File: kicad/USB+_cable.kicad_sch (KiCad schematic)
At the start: 2 parts, among them J1601 USB_C_Receptacle, J1602 USB_C_Receptacle

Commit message: Broke down sensor block into a tree of sheets
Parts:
- added D1601: GREEN, YELLOW, KwanSystems:LEDKingbrightAPHB, symbol Device:LED_Dual_AKAK
- added R1601: 330, Resistor_SMD:R_0402_1005Metric, symbol KwanSystems:RESISTOR
- added R1602: 1k, Resistor_SMD:R_0402_1005Metric, symbol KwanSystems:RESISTOR
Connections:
- net P_3V3: now also D1601.1 (A1), R1602.2
- net P_GND: now also R1601.2
- net P_ID: now also D1601.3 (A2)
- new net DG-: D1601.2 (K1), R1601.1
- new net DY-: D1601.4 (K2), R1602.1
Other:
- note added: "Will light GREEN if HI board (green=higher energy photon) YELLOW if LO board (yellow=lower energy photon) Neither color is red, so no danger/stop indication"
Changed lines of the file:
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@@
 (kicad_sch (version 20211123) (generator eeschema)
   (paper "A4")
+  (junction (at 124.46 119.38) (diameter 0) (color 0 0 0 0)
+  )
   (junction (at 213.36 129.54) (diameter 0) (color 0 0 0 0)
   )
+  (junction (at 134.62 119.38) (diameter 0) (color 0 0 0 0)
+  )
+  (junction (at 119.38 129.54) (diameter 0) (color 0 0 0 0)
+  )
   (junction (at 228.6 78.74) (diameter 0) (color 0 0 0 0)
+  )
+  (junction (at 129.54 114.3) (diameter 0) (color 0 0 0 0)
   )
   (junction (at 228.6 81.28) (diameter 0) (color 0 0 0 0)
@@
     (stroke (width 0) (type default) (color 0 0 0 0))
   )
+  (wire (pts (xy 134.62 119.38) (xy 124.46 119.38))
+    (stroke (width 0) (type default) (color 0 0 0 0))
+  )
   (polyline (pts (xy 165.1 121.92) (xy 177.8 121.92))
     (stroke (width 0) (type solid) (color 0 0 0 0))
@@
     (stroke (width 0) (type solid) (color 0 0 0 0))
   )
+  (wire (pts (xy 119.38 129.54) (xy 119.38 139.7))
+    (stroke (width 0) (type default) (color 0 0 0 0))
+  )
   (polyline (pts (xy 177.8 68.58) (xy 177.8 69.85))
     (stroke (width 0) (type solid) (color 0 0 0 0))
@@
     (stroke (width 0) (type default) (color 0 0 0 0))
   )
+  (wire (pts (xy 129.54 154.94) (xy 134.62 154.94))
+    (stroke (width 0) (type default) (color 0 0 0 0))
+  )
   (polyline (pts (xy 165.1 106.68) (xy 177.8 106.68))
     (stroke (width 0) (type solid) (color 0 0 0 0))
@@
     (stroke (width 0) (type default) (color 0 0 0 0))
   )
-  (wire (pts (xy 139.7 119.38) (xy 114.3 119.38))
+  (wire (pts (xy 124.46 119.38) (xy 114.3 119.38))
+    (stroke (width 0) (type default) (color 0 0 0 0))
+  )
+  (wire (pts (xy 139.7 119.38) (xy 134.62 119.38))
     (stroke (width 0) (type default) (color 0 0 0 0))
   )
@@
     (stroke (width 0) (type default) (color 0 0 0 0))
   )
+  (wire (pts (xy 134.62 119.38) (xy 134.62 139.7))
+    (stroke (width 0) (type default) (color 0 0 0 0))
+  )
+  (wire (pts (xy 119.38 154.94) (xy 124.46 154.94))
+    (stroke (width 0) (type default) (color 0 0 0 0))
+  )
+  (wire (pts (xy 124.46 119.38) (xy 124.46 139.7))
+    (stroke (width 0) (type default) (color 0 0 0 0))
+  )
   (wire (pts (xy 228.6 114.3) (xy 254 114.3))
     (stroke (width 0) (type default) (color 0 0 0 0))
@@
     (stroke (width 0) (type solid) (color 0 0 0 0))
   )
-  (wire (pts (xy 114.3 114.3) (xy 139.7 114.3))
+  (wire (pts (xy 134.62 154.94) (xy 134.62 144.78))
+    (stroke (width 0) (type default) (color 0 0 0 0))
+  )
+  (wire (pts (xy 114.3 114.3) (xy 129.54 114.3))
     (stroke (width 0) (type default) (color 0 0 0 0))
   )
@@
     (stroke (width 0) (type solid) (color 0 0 0 0))
   )
+  (wire (pts (xy 119.38 144.78) (xy 119.38 154.94))
+    (stroke (width 0) (type default) (color 0 0 0 0))
+  )
+  (wire (pts (xy 129.54 114.3) (xy 129.54 139.7))
+    (stroke (width 0) (type default) (color 0 0 0 0))
+  )
   (polyline (pts (xy 177.8 114.3) (xy 190.5 106.68))
     (stroke (width 0) (type solid) (color 0 0 0 0))
@@
     (stroke (width 0) (type default) (color 0 0 0 0))
   )
-  (wire (pts (xy 114.3 129.54) (xy 154.94 129.54))
+  (wire (pts (xy 114.3 129.54) (xy 119.38 129.54))
     (stroke (width 0) (type default) (color 0 0 0 0))
   )
@@
     (stroke (width 0) (type solid) (color 0 0 0 0))
   )
+  (wire (pts (xy 129.54 114.3) (xy 139.7 114.3))
+    (stroke (width 0) (type default) (color 0 0 0 0))
+  )
   (wire (pts (xy 228.6 121.92) (xy 254 121.92))
+    (stroke (width 0) (type default) (color 0 0 0 0))
+  )
+  (wire (pts (xy 119.38 129.54) (xy 154.94 129.54))
     (stroke (width 0) (type default) (color 0 0 0 0))
   )
@@
   )
   (text "BRAID" (at 181.61 125.73 0)
+    (effects (font (size 1.27 1.27)) (justify left bottom))
+  )
+  (text "Will light GREEN if HI board (green=higher energy photon)\nYELLOW if LO board (yellow=lower energy photon)\nNeither color is red, so no danger/stop indication"
+    (at 140.97 158.75 0)
     (effects (font (size 1.27 1.27)) (justify left bottom))
   )
@@
   )
   (text "WHITE(GREEN MYLAR)" (at 165.1 111.76 0)
+    (effects (font (size 1.27 1.27)) (justify left bottom))
+  )
+  (label "DY-" (at 134.62 154.94 90)
+    (effects (font (size 1.27 1.27)) (justify left bottom))
+  )
+  (label "DG-" (at 119.38 154.94 90)
     (effects (font (size 1.27 1.27)) (justify left bottom))
   )
@@
     (pin "S1")
   )
+  (symbol (lib_id "Device:LED_Dual_AKAK") (at 127 147.32 90) (mirror x)
+    (in_bom yes) (on_board yes)
+    (property "Reference" "D1601" (id 0) (at 124.46 156.21 90)
+      (effects (font (size 1.27 1.27)) (justify right))
+    )
+    (property "Value" "GREEN, YELLOW" (id 1) (at 120.65 158.75 90)
+      (effects (font (size 1.27 1.27)) (justify right))
+    )
+    (property "Footprint" "KwanSystems:LEDKingbrightAPHB" (id 2) (at 127 148.082 0)
+      (effects (font (size 1.27 1.27)) hide)
+    )
+    (property "Datasheet" "~" (id 3) (at 127 148.082 0)
+      (effects (font (size 1.27 1.27)) hide)
+    )
+    (property "Digikey" "754-1956-1-ND" (id 4) (at 127 147.32 0)
+      (effects (font (size 1.27 1.27)) hide)
+    )
+    (pin "1")
+    (pin "2")
+    (pin "3")
+    (pin "4")
+  )
+  (symbol (lib_id "KwanSystems:RESISTOR") (at 119.38 142.24 90)
+    (in_bom yes) (on_board yes)
+    (property "Reference" "R1601" (id 0) (at 118.11 144.78 0)
+      (effects (font (size 1.143 1.143)) (justify right))
+    )
+    (property "Value" "330" (id 1) (at 118.11 137.16 0)
+      (effects (font (size 1.143 1.143)) (justify right))
+    )
+    (property "Footprint" "Resistor_SMD:R_0402_1005Metric" (id 2) (at 115.57 140.843 0)
+      (effects (font (size 0.508 0.508)) hide)
+    )
+    (property "Datasheet" "" (id 3) (at 127 131.445 0)
+      (effects (font (size 1.524 1.524)) hide)
+    )
+    (pin "1")
+    (pin "2")
+  )
   (symbol (lib_id "Connector:USB_C_Receptacle") (at 213.36 88.9 0)
     (in_bom yes) (on_board yes) (fields_autoplaced)
@@
     (pin "S1")
   )
+  (symbol (lib_id "KwanSystems:RESISTOR") (at 134.62 142.24 90)
+    (in_bom yes) (on_board yes)
+    (property "Reference" "R1602" (id 0) (at 135.89 144.78 0)
+      (effects (font (size 1.143 1.143)) (justify right))
+    )
+    (property "Value" "1k" (id 1) (at 135.89 137.16 0)
+      (effects (font (size 1.143 1.143)) (justify right))
+    )
+    (property "Footprint" "Resistor_SMD:R_0402_1005Metric" (id 2) (at 130.81 140.843 0)
+      (effects (font (size 0.508 0.508)) hide)
+    )
+    (property "Datasheet" "" (id 3) (at 142.24 131.445 0)
+      (effects (font (size 1.524 1.524)) hide)
+    )
+    (pin "1")
+    (pin "2")
+  )
 )

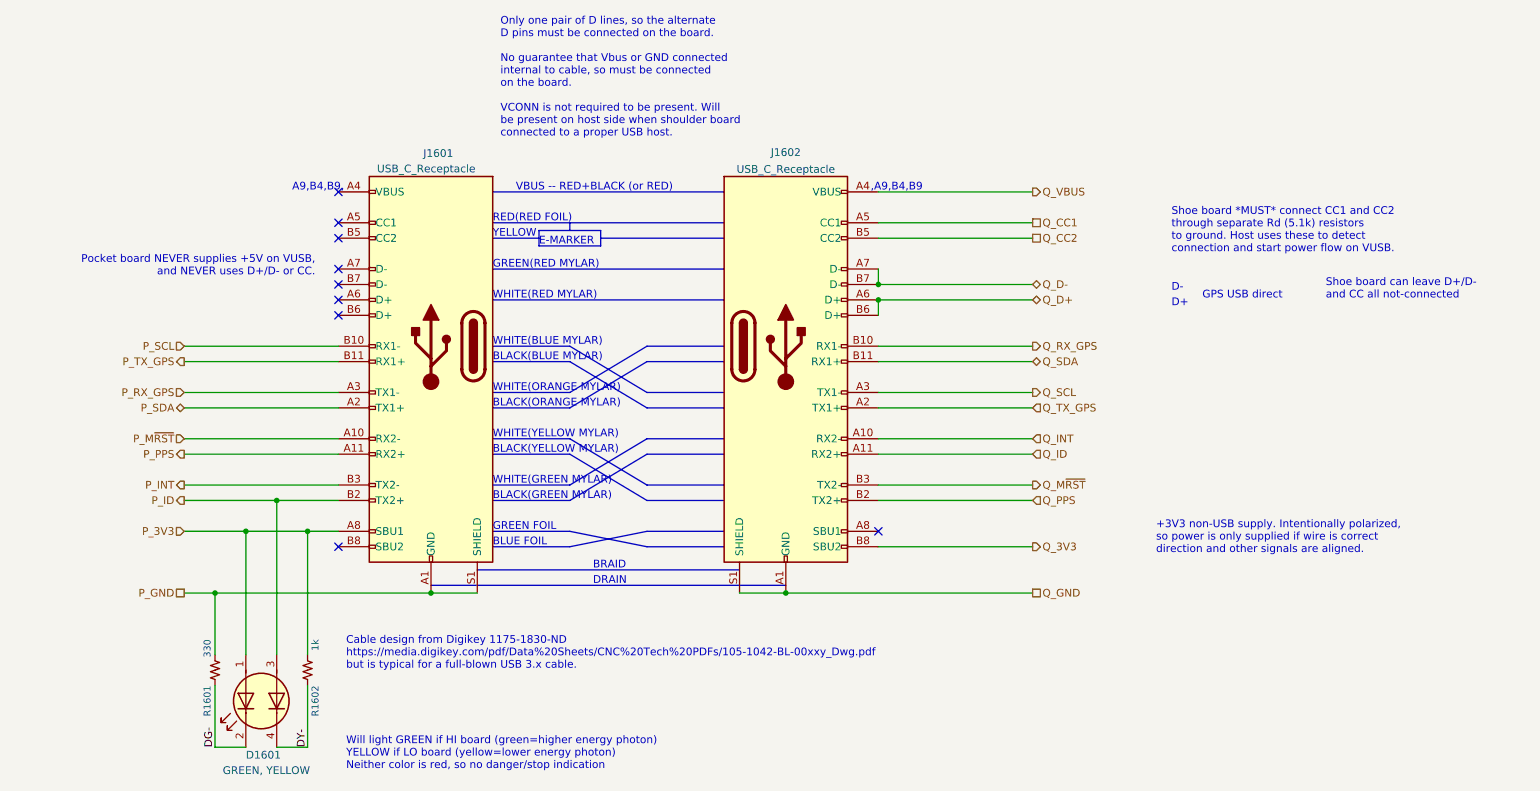
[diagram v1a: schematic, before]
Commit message: One shining moment
Commit board while it still works
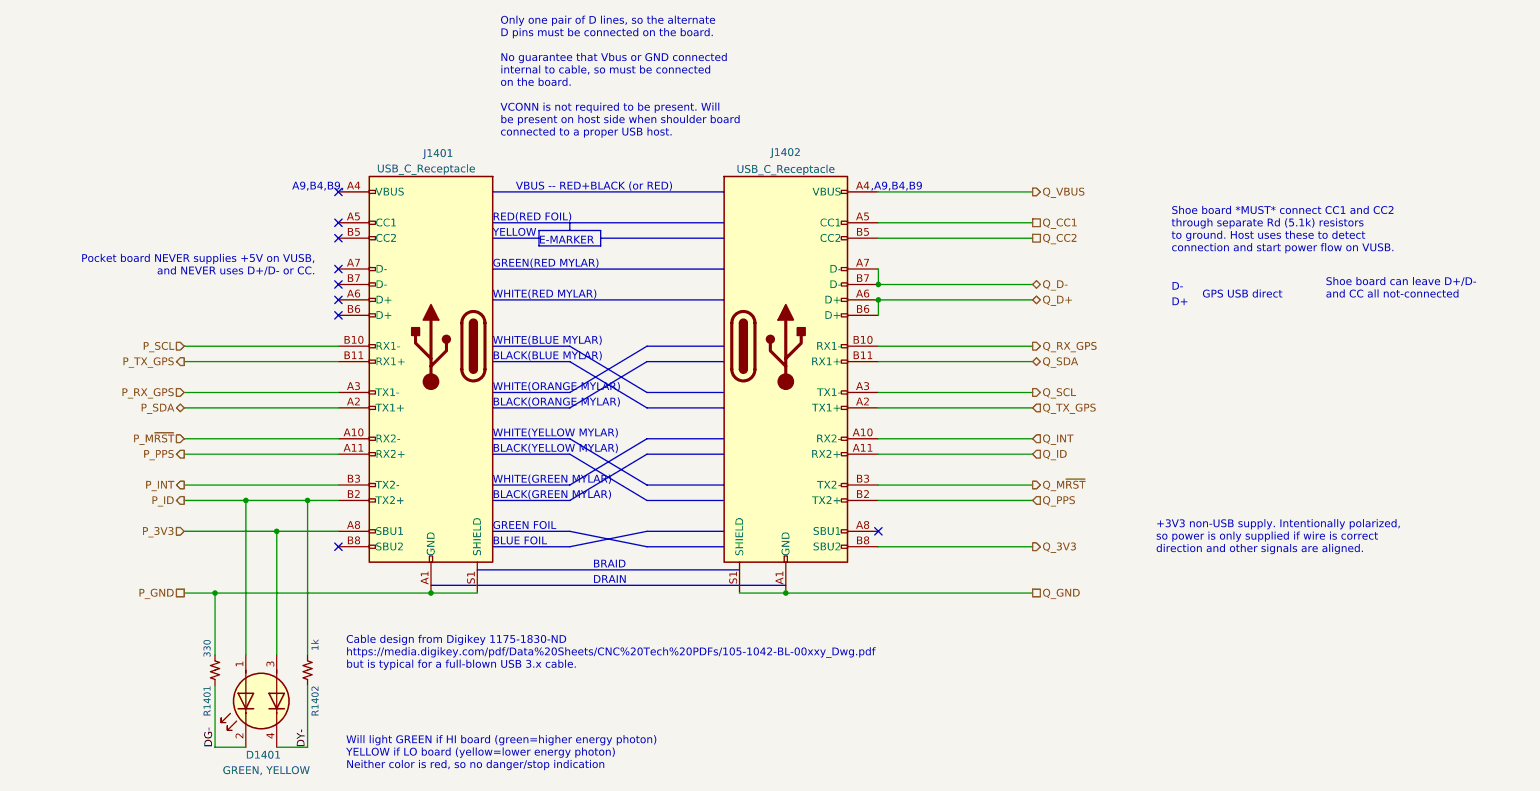
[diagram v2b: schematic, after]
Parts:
- D1401: renamed from D1601; Purpose (none) -> Remote ID indicator
- renumbered J1601 to J1401, J1602 to J1402, R1601 to R1401, R1602 to R1402
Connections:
- net P_3V3: now also D1401.3 (A2); no longer D1401.1 (A1), R1402.2
- net P_ID: now also D1401.1 (A1), R1402.2; no longer D1401.3 (A2)
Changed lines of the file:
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@@
 (kicad_sch (version 20211123) (generator eeschema)
   (paper "A4")
-  (junction (at 124.46 119.38) (diameter 0) (color 0 0 0 0)
-  )
   (junction (at 213.36 129.54) (diameter 0) (color 0 0 0 0)
   )
-  (junction (at 134.62 119.38) (diameter 0) (color 0 0 0 0)
-  )
   (junction (at 119.38 129.54) (diameter 0) (color 0 0 0 0)
   )
   (junction (at 228.6 78.74) (diameter 0) (color 0 0 0 0)
   )
-  (junction (at 129.54 114.3) (diameter 0) (color 0 0 0 0)
+  (junction (at 134.62 114.3) (diameter 0) (color 0 0 0 0)
   )
   (junction (at 228.6 81.28) (diameter 0) (color 0 0 0 0)
+  )
+  (junction (at 129.54 119.38) (diameter 0) (color 0 0 0 0)
+  )
+  (junction (at 124.46 114.3) (diameter 0) (color 0 0 0 0)
   )
   (junction (at 154.94 129.54) (diameter 0) (color 0 0 0 0)
@@
     (stroke (width 0) (type default) (color 0 0 0 0))
   )
+  (wire (pts (xy 129.54 119.38) (xy 139.7 119.38))
+    (stroke (width 0) (type default) (color 0 0 0 0))
+  )
   (polyline (pts (xy 172.72 69.85) (xy 172.72 72.39))
     (stroke (width 0) (type solid) (color 0 0 0 0))
@@
     (stroke (width 0) (type default) (color 0 0 0 0))
   )
+  (wire (pts (xy 119.38 129.54) (xy 154.94 129.54))
+    (stroke (width 0) (type default) (color 0 0 0 0))
+  )
   (polyline (pts (xy 190.5 88.9) (xy 203.2 88.9))
     (stroke (width 0) (type solid) (color 0 0 0 0))
   )
+  (wire (pts (xy 134.62 114.3) (xy 134.62 139.7))
+    (stroke (width 0) (type default) (color 0 0 0 0))
+  )
   (wire (pts (xy 114.3 106.68) (xy 139.7 106.68))
     (stroke (width 0) (type default) (color 0 0 0 0))
   )
-  (wire (pts (xy 134.62 119.38) (xy 124.46 119.38))
+  (wire (pts (xy 114.3 119.38) (xy 129.54 119.38))
     (stroke (width 0) (type default) (color 0 0 0 0))
   )
@@
     (stroke (width 0) (type solid) (color 0 0 0 0))
   )
+  (wire (pts (xy 134.62 114.3) (xy 139.7 114.3))
+    (stroke (width 0) (type default) (color 0 0 0 0))
+  )
   (polyline (pts (xy 190.5 114.3) (xy 203.2 114.3))
     (stroke (width 0) (type solid) (color 0 0 0 0))
@@
     (stroke (width 0) (type default) (color 0 0 0 0))
   )
+  (wire (pts (xy 129.54 119.38) (xy 129.54 139.7))
+    (stroke (width 0) (type default) (color 0 0 0 0))
+  )
   (wire (pts (xy 114.3 96.52) (xy 139.7 96.52))
     (stroke (width 0) (type default) (color 0 0 0 0))
@@
     (stroke (width 0) (type default) (color 0 0 0 0))
   )
-  (wire (pts (xy 124.46 119.38) (xy 114.3 119.38))
-    (stroke (width 0) (type default) (color 0 0 0 0))
-  )
-  (wire (pts (xy 139.7 119.38) (xy 134.62 119.38))
-    (stroke (width 0) (type default) (color 0 0 0 0))
-  )
   (polyline (pts (xy 165.1 81.28) (xy 203.2 81.28))
     (stroke (width 0) (type solid) (color 0 0 0 0))
@@
     (stroke (width 0) (type default) (color 0 0 0 0))
   )
-  (wire (pts (xy 134.62 119.38) (xy 134.62 139.7))
-    (stroke (width 0) (type default) (color 0 0 0 0))
-  )
   (wire (pts (xy 119.38 154.94) (xy 124.46 154.94))
     (stroke (width 0) (type default) (color 0 0 0 0))
   )
-  (wire (pts (xy 124.46 119.38) (xy 124.46 139.7))
-    (stroke (width 0) (type default) (color 0 0 0 0))
-  )
   (wire (pts (xy 228.6 114.3) (xy 254 114.3))
     (stroke (width 0) (type default) (color 0 0 0 0))
@@
     (stroke (width 0) (type default) (color 0 0 0 0))
   )
+  (wire (pts (xy 124.46 114.3) (xy 124.46 139.7))
+    (stroke (width 0) (type default) (color 0 0 0 0))
+  )
   (wire (pts (xy 114.3 104.14) (xy 139.7 104.14))
     (stroke (width 0) (type default) (color 0 0 0 0))
@@
     (stroke (width 0) (type default) (color 0 0 0 0))
   )
-  (wire (pts (xy 114.3 114.3) (xy 129.54 114.3))
+  (wire (pts (xy 114.3 114.3) (xy 124.46 114.3))
     (stroke (width 0) (type default) (color 0 0 0 0))
   )
@@
     (stroke (width 0) (type default) (color 0 0 0 0))
   )
-  (wire (pts (xy 129.54 114.3) (xy 129.54 139.7))
-    (stroke (width 0) (type default) (color 0 0 0 0))
-  )
   (polyline (pts (xy 177.8 114.3) (xy 190.5 106.68))
     (stroke (width 0) (type solid) (color 0 0 0 0))
@@
     (stroke (width 0) (type solid) (color 0 0 0 0))
   )
-  (wire (pts (xy 129.54 114.3) (xy 139.7 114.3))
+  (wire (pts (xy 124.46 114.3) (xy 134.62 114.3))
     (stroke (width 0) (type default) (color 0 0 0 0))
   )
   (wire (pts (xy 228.6 121.92) (xy 254 121.92))
-    (stroke (width 0) (type default) (color 0 0 0 0))
-  )
-  (wire (pts (xy 119.38 129.54) (xy 154.94 129.54))
     (stroke (width 0) (type default) (color 0 0 0 0))
   )
@@
   (symbol (lib_id "Connector:USB_C_Receptacle") (at 154.94 88.9 0) (mirror y)
     (in_bom yes) (on_board yes)
-    (property "Reference" "J1601" (id 0) (at 153.67 57.15 0)
+    (property "Reference" "J1401" (id 0) (at 153.67 57.15 0)
       (effects (font (size 1.27 1.27)) (justify right))
     )
@@
   (symbol (lib_id "Device:LED_Dual_AKAK") (at 127 147.32 90) (mirror x)
     (in_bom yes) (on_board yes)
-    (property "Reference" "D1601" (id 0) (at 124.46 156.21 90)
+    (property "Reference" "D1401" (id 0) (at 124.46 156.21 90)
       (effects (font (size 1.27 1.27)) (justify right))
     )
@@
     )
     (property "Digikey" "754-1956-1-ND" (id 4) (at 127 147.32 0)
+      (effects (font (size 1.27 1.27)) hide)
+    )
+    (property "Purpose" "Remote ID indicator" (id 5) (at 127 147.32 0)
       (effects (font (size 1.27 1.27)) hide)
     )
@@
   (symbol (lib_id "KwanSystems:RESISTOR") (at 119.38 142.24 90)
     (in_bom yes) (on_board yes)
-    (property "Reference" "R1601" (id 0) (at 118.11 144.78 0)
+    (property "Reference" "R1401" (id 0) (at 118.11 144.78 0)
       (effects (font (size 1.143 1.143)) (justify right))
     )
@@
   (symbol (lib_id "Connector:USB_C_Receptacle") (at 213.36 88.9 0)
     (in_bom yes) (on_board yes) (fields_autoplaced)
-    (property "Reference" "J1602" (id 0) (at 213.36 56.9935 0))
+    (property "Reference" "J1402" (id 0) (at 213.36 56.9935 0))
     (property "Value" "USB_C_Receptacle" (id 1) (at 213.36 59.7686 0))
     (property "Footprint" "KwanSystems:USB_C_Amphenol_MidMount" (id 2) (at 217.17 88.9 0)
@@
   (symbol (lib_id "KwanSystems:RESISTOR") (at 134.62 142.24 90)
     (in_bom yes) (on_board yes)
-    (property "Reference" "R1602" (id 0) (at 135.89 144.78 0)
+    (property "Reference" "R1402" (id 0) (at 135.89 144.78 0)
       (effects (font (size 1.143 1.143)) (justify right))
     )

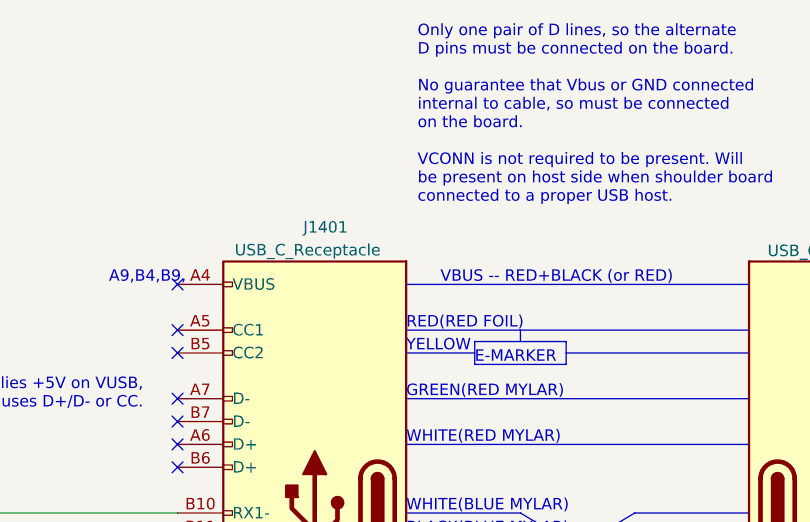
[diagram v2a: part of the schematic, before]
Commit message: Edited symbol to remove ERC violations
Some of the overlapping NC pins were getting connected through the NC symbol (not connected to anything else, but connected to each other). This is fixed by editing this instance of the symbol and offsetting the pins from each other.
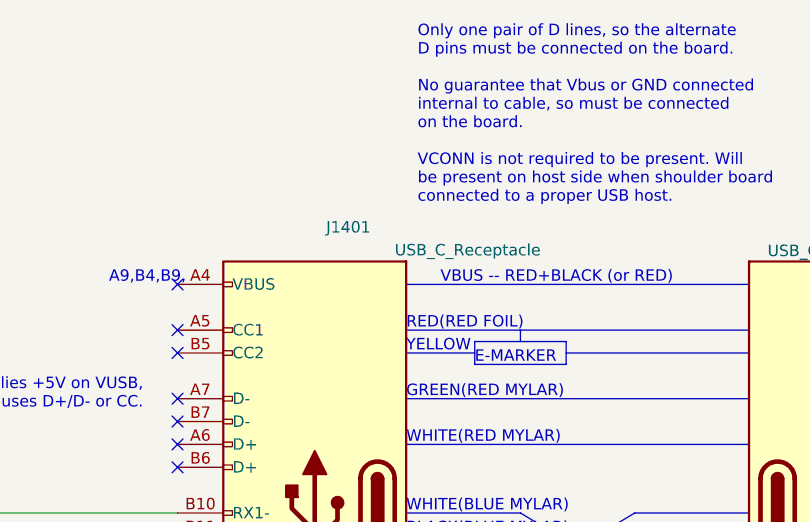
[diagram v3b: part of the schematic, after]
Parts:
- J1401: Digikey WM12856CT-ND -> 664-12402072E512ACT-ND
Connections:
- now unconnected: J1401.A4 (VBUS)
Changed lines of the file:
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@@
     (effects (font (size 1.27 1.27)) (justify right))
   )
-  (symbol (lib_id "Connector:USB_C_Receptacle") (at 154.94 88.9 0) (mirror y)
+  (symbol (lib_name "USB_C_Receptacle_1") (lib_id "Connector:USB_C_Receptacle") (at 154.94 88.9 0) (mirror y)
     (in_bom yes) (on_board yes)
-    (property "Reference" "J1401" (id 0) (at 153.67 57.15 0)
+    (property "Reference" "J1401" (id 0) (at 156.21 57.15 0)
       (effects (font (size 1.27 1.27)) (justify right))
     )
-    (property "Value" "USB_C_Receptacle" (id 1) (at 146.05 59.69 0)
+    (property "Value" "USB_C_Receptacle" (id 1) (at 163.83 59.69 0)
       (effects (font (size 1.27 1.27)) (justify right))
     )
-    (property "Footprint" "KwanSystems:USB_C_Amphenol_MidMount" (id 2) (at 151.13 88.9 0)
+    (property "Footprint" "KwanSystems:USB_C_Amphenol_MidMount" (id 2) (at 158.75 88.9 0)
       (effects (font (size 1.27 1.27)) hide)
     )
-    (property "Datasheet" "https://www.usb.org/sites/default/files/documents/usb_type-c.zip" (id 3) (at 151.13 88.9 0)
+    (property "Datasheet" "https://www.usb.org/sites/default/files/documents/usb_type-c.zip" (id 3) (at 158.75 88.9 0)
       (effects (font (size 1.27 1.27)) hide)
     )
@@
       (effects (font (size 1.27 1.27)) hide)
     )
-    (property "Digikey" "WM12856CT-ND" (id 5) (at 154.94 88.9 0)
+    (property "Digikey" "664-12402072E512ACT-ND" (id 5) (at 154.94 88.9 0)
       (effects (font (size 1.27 1.27)) hide)
     )
@@
     (pin "A7")
     (pin "A8")
-    (pin "A9")
     (pin "B1")
     (pin "B10")
@@
     (pin "B2")
     (pin "B3")
-    (pin "B4")
     (pin "B5")
     (pin "B6")
     (pin "B7")
     (pin "B8")
-    (pin "B9")
     (pin "S1")
   )
